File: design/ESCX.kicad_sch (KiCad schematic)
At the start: 11 parts, among them J1 SWD

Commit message: Agregue LCSC Part #
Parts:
- R1, R2: LCSC (none) -> C107696
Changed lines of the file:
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@@
+			)
+		)
+		(property "LCSC" "C107696"
+			(at 184.15 142.24 0)
+			(effects
+				(font
+					(size 1.27 1.27)
+				)
+				(hide yes)
 			)
 		)
@@
 			(at 184.15 146.05 0)
 			(effects
+				(font
+					(size 1.27 1.27)
+				)
+				(hide yes)
+			)
+		)
+		(property "LCSC" "C107696"
+			(at 184.15 146.05 0)
+			(effects

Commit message: Agregue LCSC Part # a algunas resistencias
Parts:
- R3: LCSC (none) -> C22548
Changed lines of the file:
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@@
+			)
+		)
+		(property "LCSC" "C22548"
+			(at 195.58 135.89 0)
+			(effects
+				(font
+					(size 1.27 1.27)
+				)
+				(hide yes)
 			)
 		)

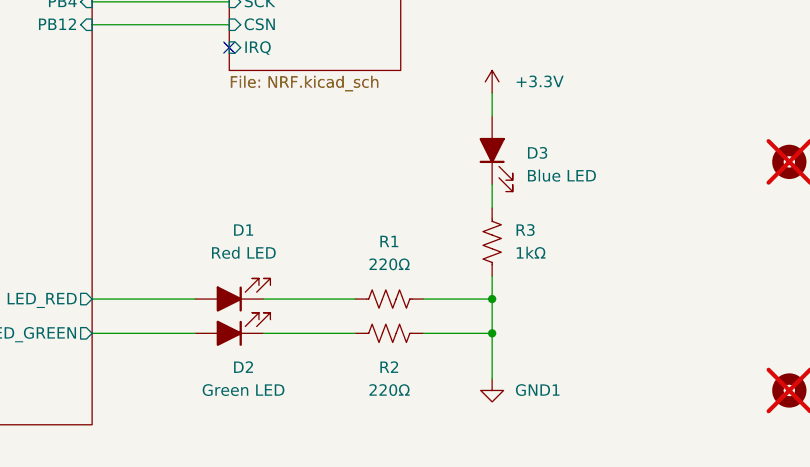
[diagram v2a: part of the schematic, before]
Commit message: Abaratando costos
Cambios en numeros de jlcpcb, pasados a componentes básicos
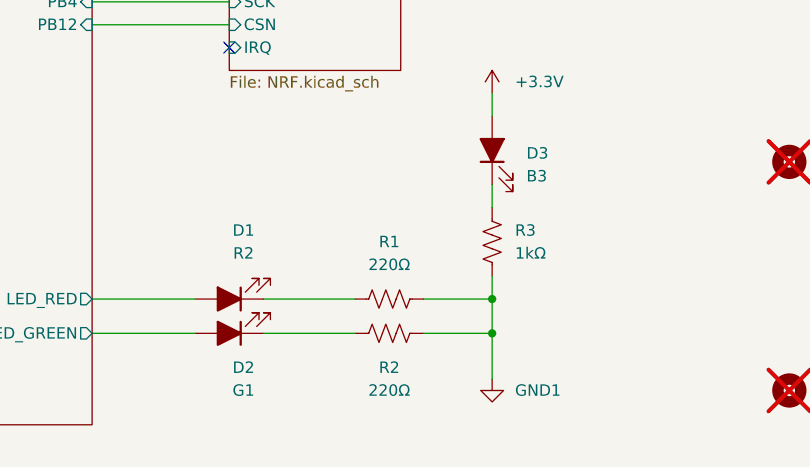
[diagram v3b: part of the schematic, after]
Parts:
- D1: value Red LED -> R2; LCSC C123009 -> C2286
- D2: value Green LED -> G1; LCSC C2984263 -> C2286
- D3: value Blue LED -> B3; LCSC C2846635 -> C2286
- J1: now left out of the parts list
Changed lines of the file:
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@@
 			)
 		)
-		(property "Value" "Red LED"
+		(property "Value" "R2"
 			(at 167.9575 137.16 0)
 			(effects
@@
 			)
 		)
-		(property "LCSC" "C123009"
+		(property "LCSC" "C2286"
 			(at 167.9575 134.62 0)
 			(effects
@@
 			)
 		)
-		(property "Value" "Green LED"
+		(property "Value" "G1"
 			(at 167.9575 152.4 0)
 			(effects
@@
 			)
 		)
-		(property "LCSC" "C2984263"
+		(property "LCSC" "C2286"
 			(at 167.9575 149.86 0)
 			(effects
@@
 			)
 		)
-		(property "Value" "Blue LED"
+		(property "Value" "B3"
 			(at 199.39 128.5874 90)
 			(effects
@@
 			)
 		)
-		(property "LCSC" "C2846635"
+		(property "LCSC" "C2286"
 			(at 199.39 126.0474 0)
 			(effects
@@
 		(unit 1)
 		(exclude_from_sim no)
-		(in_bom yes)
+		(in_bom no)
 		(on_board yes)
 		(dnp no)

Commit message: cambie resistencias a basic
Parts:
- R1, R2: LCSC C107696 -> C1226; MPN RC0603FR-07220RL -> 0603WAJ0221T5E; Manufacturer YAGEO -> UNI-ROYAL(Uniroyal Elec)
- R3: LCSC C22548 -> C21190; MPN RC0603FR-071KL -> 0603WAF1001T5E; Manufacturer YAGEO -> UNI-ROYAL(Uniroyal Elec)
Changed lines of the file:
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@@
 			)
 		)
-		(property "Manufacturer" "YAGEO"
+		(property "Manufacturer" "UNI-ROYAL(Uniroyal Elec)"
 			(at 184.15 142.24 0)
 			(effects
@@
 			)
 		)
-		(property "MPN" "RC0603FR-07220RL"
+		(property "MPN" "0603WAJ0221T5E"
 			(at 184.15 142.24 0)
 			(effects
@@
 			)
 		)
-		(property "LCSC" "C107696"
+		(property "LCSC" "C1226"
 			(at 184.15 142.24 0)
 			(effects
@@
 			)
 		)
-		(property "Manufacturer" "YAGEO"
+		(property "Manufacturer" "UNI-ROYAL(Uniroyal Elec)"
 			(at 184.15 146.05 0)
 			(effects
@@
 			)
 		)
-		(property "MPN" "RC0603FR-07220RL"
+		(property "MPN" "0603WAJ0221T5E"
 			(at 184.15 146.05 0)
 			(effects
@@
 			)
 		)
-		(property "LCSC" "C107696"
+		(property "LCSC" "C1226"
 			(at 184.15 146.05 0)
 			(effects
@@
 			)
 		)
-		(property "Manufacturer" "YAGEO"
+		(property "Manufacturer" "UNI-ROYAL(Uniroyal Elec)"
 			(at 195.58 135.89 0)
 			(effects
@@
 			)
 		)
-		(property "MPN" "RC0603FR-071KL"
+		(property "MPN" "0603WAF1001T5E"
 			(at 195.58 135.89 0)
 			(effects
@@
 			)
 		)
-		(property "LCSC" "C22548"
+		(property "LCSC" "C21190"
 			(at 195.58 135.89 0)
 			(effects

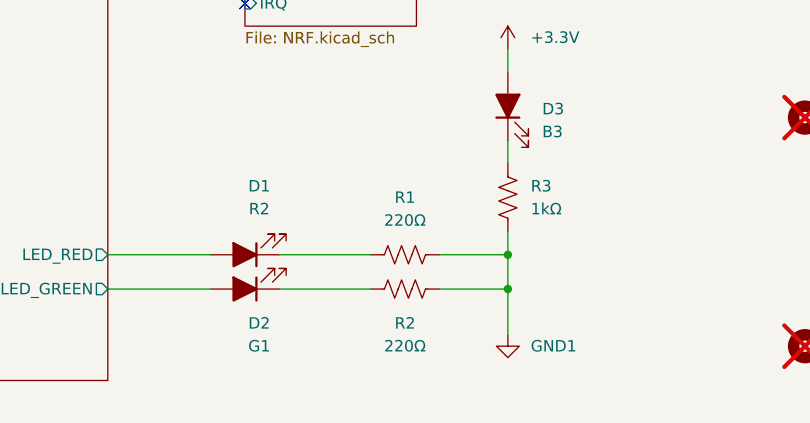
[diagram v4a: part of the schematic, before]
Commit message: cambios en la BOM
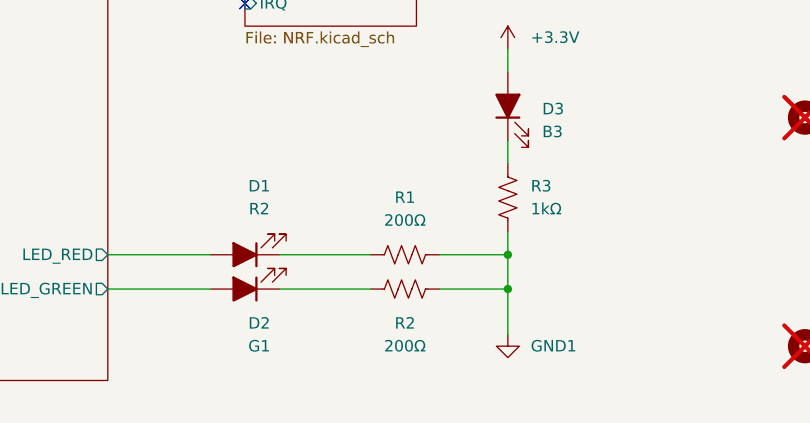
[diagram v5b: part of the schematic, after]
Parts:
- R1, R2: value 220Ω -> 200Ω; LCSC C1226 -> C8218; MPN 0603WAJ0221T5E -> 0603WAF2000T5E
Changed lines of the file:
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@@
 			)
 		)
-		(property "Value" "220Ω"
+		(property "Value" "200Ω"
 			(at 184.15 138.43 90)
 			(effects
@@
 			)
 		)
-		(property "MPN" "0603WAJ0221T5E"
+		(property "MPN" "0603WAF2000T5E"
 			(at 184.15 142.24 0)
 			(effects
@@
 			)
 		)
-		(property "LCSC" "C1226"
+		(property "LCSC" "C8218"
 			(at 184.15 142.24 0)
 			(effects
@@
 			)
 		)
-		(property "Value" "220Ω"
+		(property "Value" "200Ω"
 			(at 184.15 152.4 90)
 			(effects
@@
 			)
 		)
-		(property "MPN" "0603WAJ0221T5E"
+		(property "MPN" "0603WAF2000T5E"
 			(at 184.15 146.05 0)
 			(effects
@@
 			)
 		)
-		(property "LCSC" "C1226"
+		(property "LCSC" "C8218"
 			(at 184.15 146.05 0)
 			(effects

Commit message: Cambios
Actualizado footprint de USB, cambio de capacitor de feedback por uno básico, pequeños cambios en la ubicación de los footprints.
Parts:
- D1: MPN SML-310VTT86 -> (none); Manufacturer ROHM Semicon -> (none)
- D2: MPN 19-21/G6C-FM1N2B/4T -> (none); Manufacturer Everlight Elec -> (none)
- D3: MPN SML-E13BC8TT86 -> (none); Manufacturer ROHM Semicon -> (none)
- J1: MPN HB-PH3-25415PB2GOP -> (none); Manufacturer Hanbo Electronic -> (none)
- R1, R2: MPN 0603WAF2000T5E -> (none); Manufacturer UNI-ROYAL(Uniroyal Elec) -> (none)
- R3: MPN 0603WAF1001T5E -> (none); Manufacturer UNI-ROYAL(Uniroyal Elec) -> (none)
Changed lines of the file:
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@@
-			)
-		)
-		(property "Manufacturer" "ROHM Semicon"
-			(at 166.37 142.24 0)
-			(effects
-				(font
-					(size 1.27 1.27)
-				)
-				(hide yes)
-			)
-		)
-		(property "MPN" "SML-310VTT86"
-			(at 166.37 142.24 0)
-			(effects
-				(font
-					(size 1.27 1.27)
-				)
-				(hide yes)
 			)
 		)
@@
 			)
 		)
-		(property "Manufacturer" "Everlight Elec"
-			(at 166.37 146.05 0)
-			(effects
-				(font
-					(size 1.27 1.27)
-				)
-				(hide yes)
-			)
-		)
-		(property "MPN" " 19-21/G6C-FM1N2B/4T"
-			(at 166.37 146.05 0)
-			(effects
-				(font
-					(size 1.27 1.27)
-				)
-				(hide yes)
-			)
-		)
 		(property "LCSC" "C2286"
 			(at 167.9575 149.86 0)
@@
 			)
 		)
-		(property "Manufacturer" "UNI-ROYAL(Uniroyal Elec)"
-			(at 184.15 142.24 0)
-			(effects
-				(font
-					(size 1.27 1.27)
-				)
-				(hide yes)
-			)
-		)
-		(property "MPN" "0603WAF2000T5E"
-			(at 184.15 142.24 0)
-			(effects
-				(font
-					(size 1.27 1.27)
-				)
-				(hide yes)
-			)
-		)
 		(property "LCSC" "C8218"
 			(at 184.15 142.24 0)
@@
 			)
 		)
-		(property "Manufacturer" "UNI-ROYAL(Uniroyal Elec)"
-			(at 184.15 146.05 0)
-			(effects
-				(font
-					(size 1.27 1.27)
-				)
-				(hide yes)
-			)
-		)
-		(property "MPN" "0603WAF2000T5E"
-			(at 184.15 146.05 0)
-			(effects
-				(font
-					(size 1.27 1.27)
-				)
-				(hide yes)
-			)
-		)
 		(property "LCSC" "C8218"
 			(at 184.15 146.05 0)
@@
 		)
 		(property "Description" "Light emitting diode, filled shape"
-			(at 195.58 125.73 0)
-			(effects
-				(font
-					(size 1.27 1.27)
-				)
-				(hide yes)
-			)
-		)
-		(property "Manufacturer" "ROHM Semicon"
-			(at 195.58 125.73 0)
-			(effects
-				(font
-					(size 1.27 1.27)
-				)
-				(hide yes)
-			)
-		)
-		(property "MPN" "SML-E13BC8TT86"
 			(at 195.58 125.73 0)
 			(effects
@@
 			)
 		)
-		(property "Manufacturer" " Hanbo Electronic"
-			(at 66.04 125.73 0)
-			(effects
-				(font
-					(size 1.27 1.27)
-				)
-				(hide yes)
-			)
-		)
-		(property "MPN" "HB-PH3-25415PB2GOP"
-			(at 66.04 125.73 0)
-			(effects
-				(font
-					(size 1.27 1.27)
-				)
-				(hide yes)
-			)
-		)
 		(property "LCSC" "C6332198"
 			(at 63.5 124.4599 0)
@@
 			(at 195.58 135.89 0)
 			(effects
-				(font
-					(size 1.27 1.27)
-				)
-				(hide yes)
-			)
-		)
-		(property "Manufacturer" "UNI-ROYAL(Uniroyal Elec)"
-			(at 195.58 135.89 0)
-			(effects
-				(font
-					(size 1.27 1.27)
-				)
-				(hide yes)
-			)
-		)
-		(property "MPN" "0603WAF1001T5E"
-			(at 195.58 135.89 0)
-			(effects
